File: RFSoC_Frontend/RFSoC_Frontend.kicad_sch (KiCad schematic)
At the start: 64 parts, among them J1 Conn_Coaxial, J2 Conn_Coaxial, J3 Conn_Coaxial, J4 Conn_Coaxial, J5 Conn_Coaxial, J6 Conn_Coaxial, J7 Conn_Coaxial, J8 Conn_Coaxial, U1 TCM2-33WX+, U2 TCM2-33WX+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

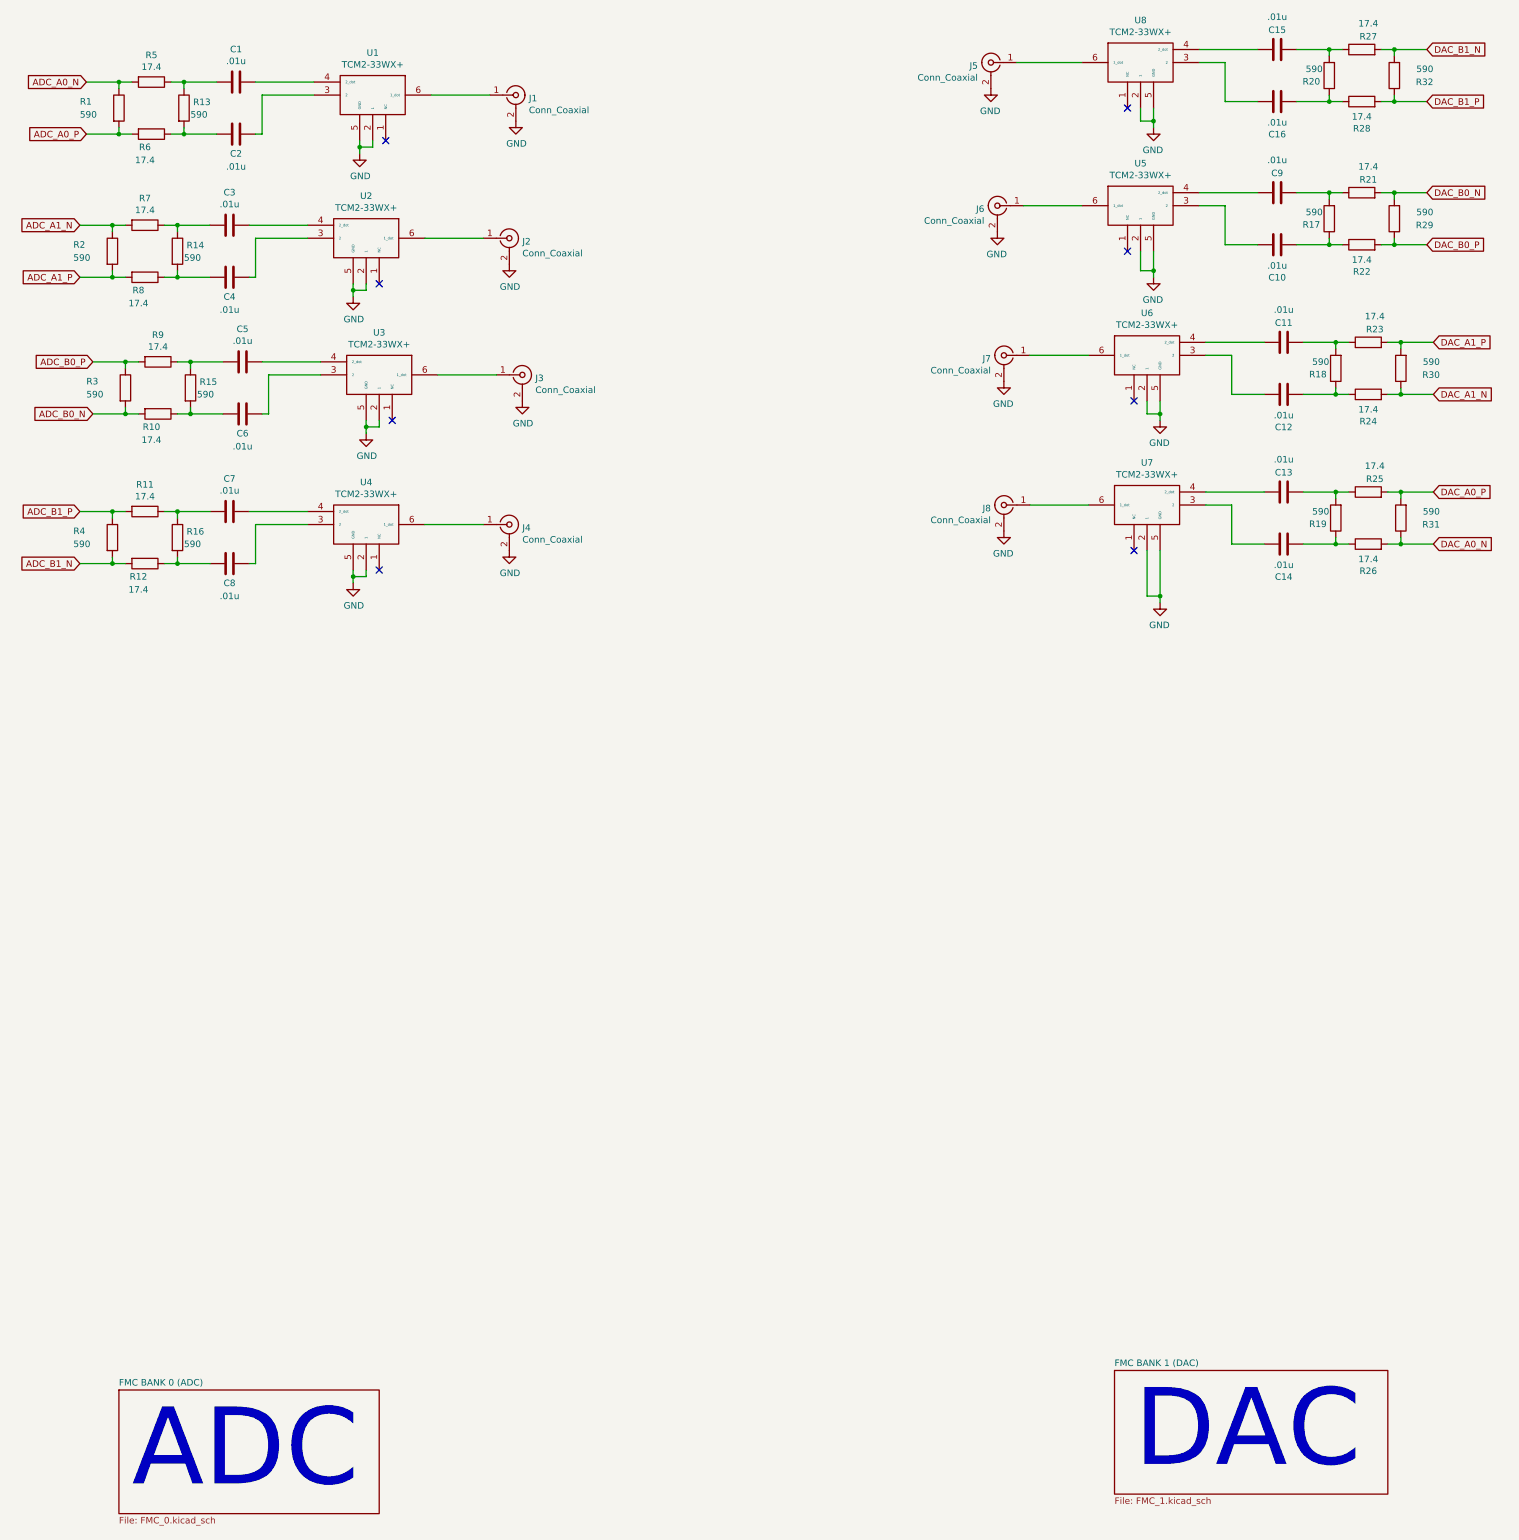
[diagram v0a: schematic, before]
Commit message: Squashed commit of the following:
commit 11c362fd04afcdda8fc54016fc262973d8ee90dd
Author: cody <you@example.com>
Date:   Sat May 14 20:18:42 2022 -0700

    updated silkscreens, degin DRC corrections

commit c03c76887280f84603892cf274eefb7fb13b0fa8
Author: cody <you@example.com>
Date:   Fri May 13 16:10:57 2022 -0700

    fork em

commit e1673cb11a9ebe940ceda00a5b2ec080c415b465
Author: cody <you@example.com>
Date:   Fri May 13 15:38:00 2022 -0700

    updated all

commit 84fbdba19d4f5d8a85804f2c5d387b833a8e7f5e
Author: Cody Roberson <carobers@asu.edu>
Date:   Mon May 9 16:15:14 2022 -0700

    Finished Updated ADC schematic

    ADC schematic was modified to match the pin map between
    the rfsoc and the xm500.

commit 1e4de3bc2e504d4b0d3d294a2c6c5a2a5a485041
Author: cody <you@example.com>
Date:   Mon May 9 10:21:30 2022 -0700

    progress check

    Started Labeling process

commit 6cadb2acb3bb1a794e84b73e4dfc828af985fa6c
Author: cody <you@example.com>
Date:   Thu May 5 15:24:15 2022 -0700

    partial update of labels

commit 2dab10b1dfa9c61606f5d562ab6e543ae0948647
Merge: 76ba8d6 79e9342
Author: Cody Roberson <codyaroberson@outlook.com>
Date:   Wed Mar 9 20:07:10 2022 -0700

    Merge pull request #1 from CodyRoberson/twochannel_clk

    Twochannel clk

commit 79e93425439f23e00c2b0d92e892590d87fe78f7
Author: Cody Roberson <carobers@asu.edu>
Date:   Wed Mar 9 20:04:09 2022 -0700

    moved forkem and labeled ports

commit 9a4b6dc66818e11f3bb9969be501559d1f9e476d
Author: Cody Roberson <carobers@asu.edu>
Date:   Wed Mar 9 16:28:24 2022 -0700

    improvements

    Made improvement to kicad symbol and replaced footprint for baluns. They
    were incorrectly orientated with regards to pin numbering

commit 8d29e46f6a613ffa86cae2f2a7a070122b97e7eb
Author: Cody Roberson <carobers@asu.edu>
Date:   Wed Mar 9 14:50:01 2022 -0700

    added kicad symbol+footprint

commit 3c7e1566d05959f7dad261469b2e27b92f79ed87
Author: Cody Roberson <carobers@asu.edu>
Date:   Wed Mar 9 14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
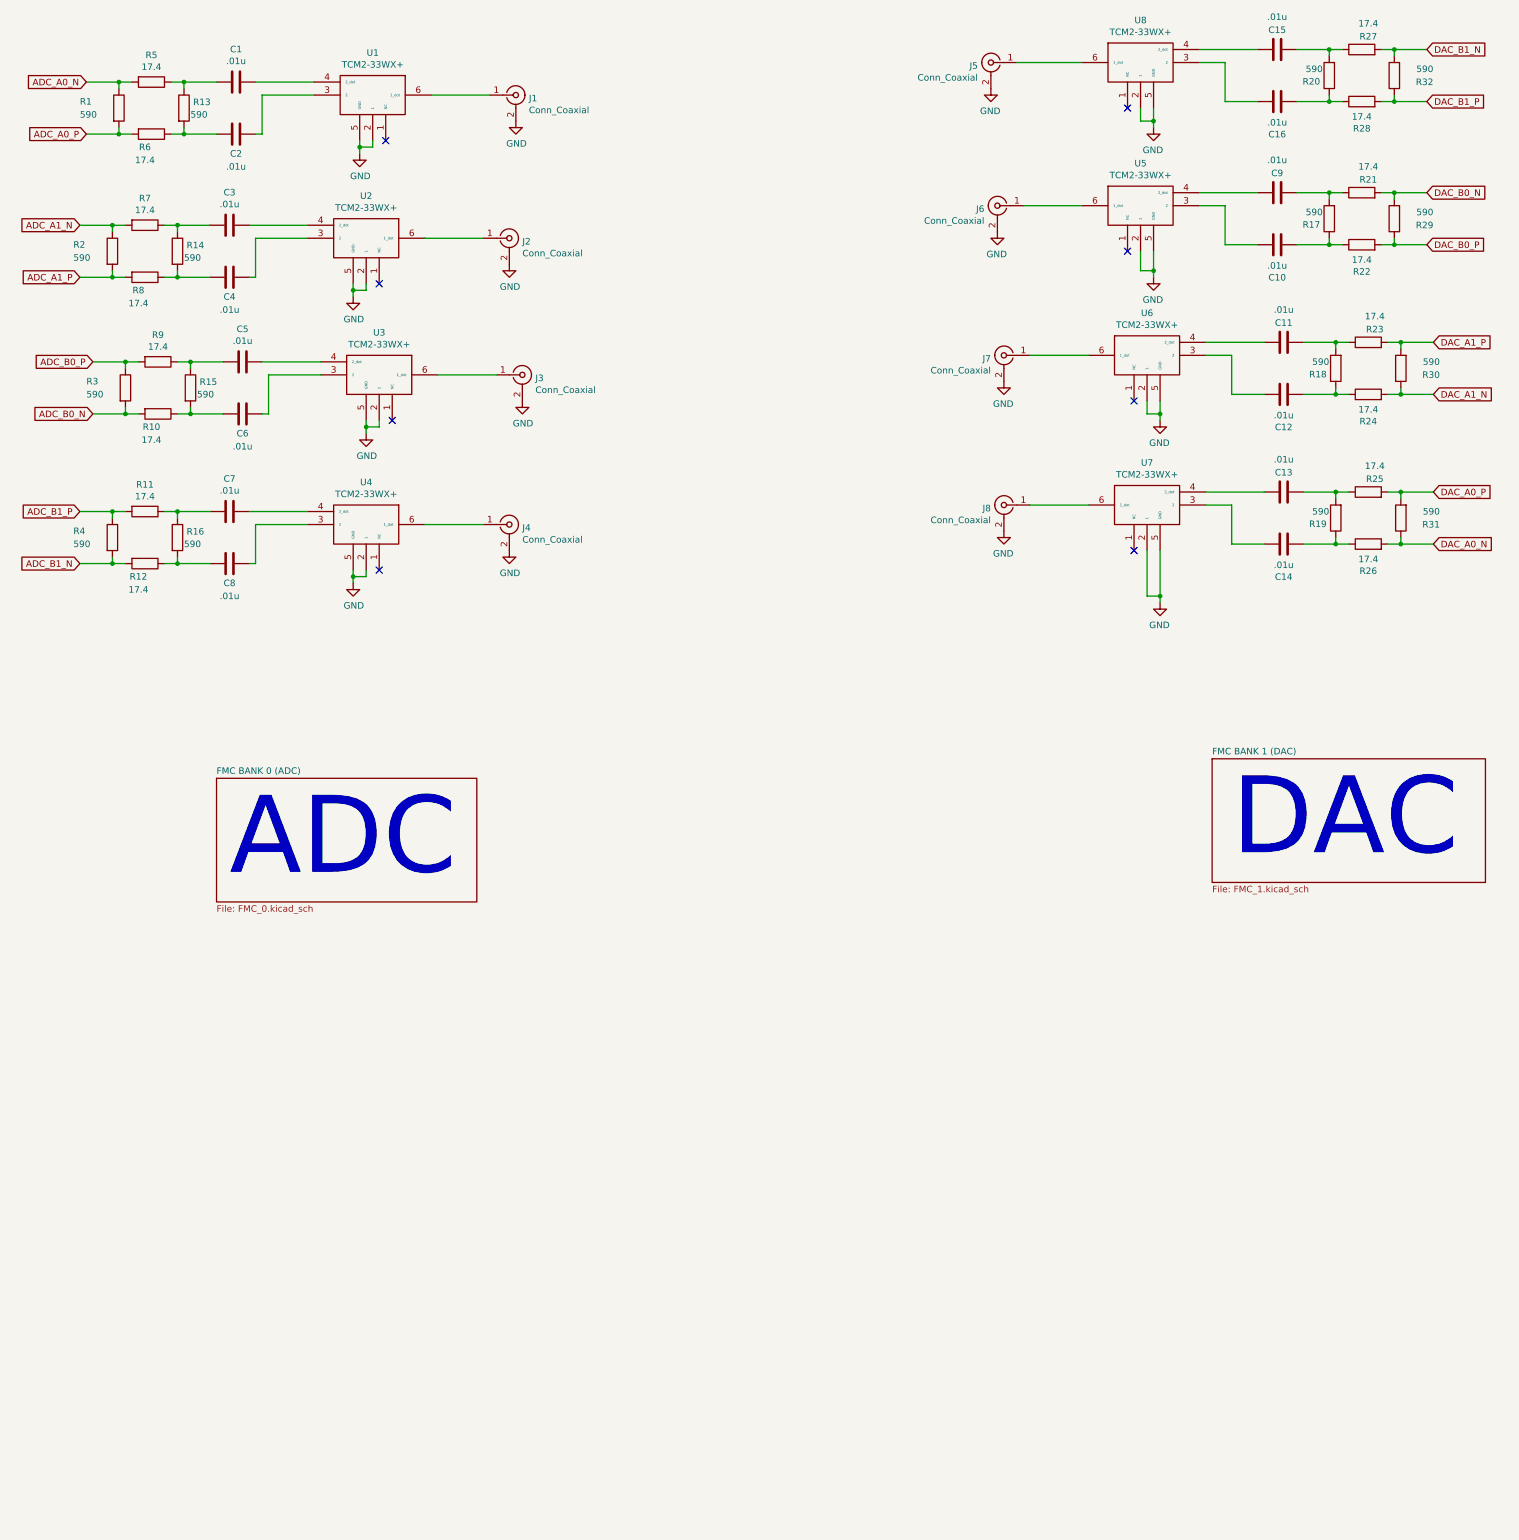
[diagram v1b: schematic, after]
